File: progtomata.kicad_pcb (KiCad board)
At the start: 2 copper layers, 29 parts, among them J1 Conn_01x04_Pin, J2 Conn_01x04_Pin, P1 USB_C_Plug_USB2.0, SW1 SW_SPDT, U1 STM32F407VGTx, U2 AMS1117-3.3, U3 74LS148, Y1 8MHz

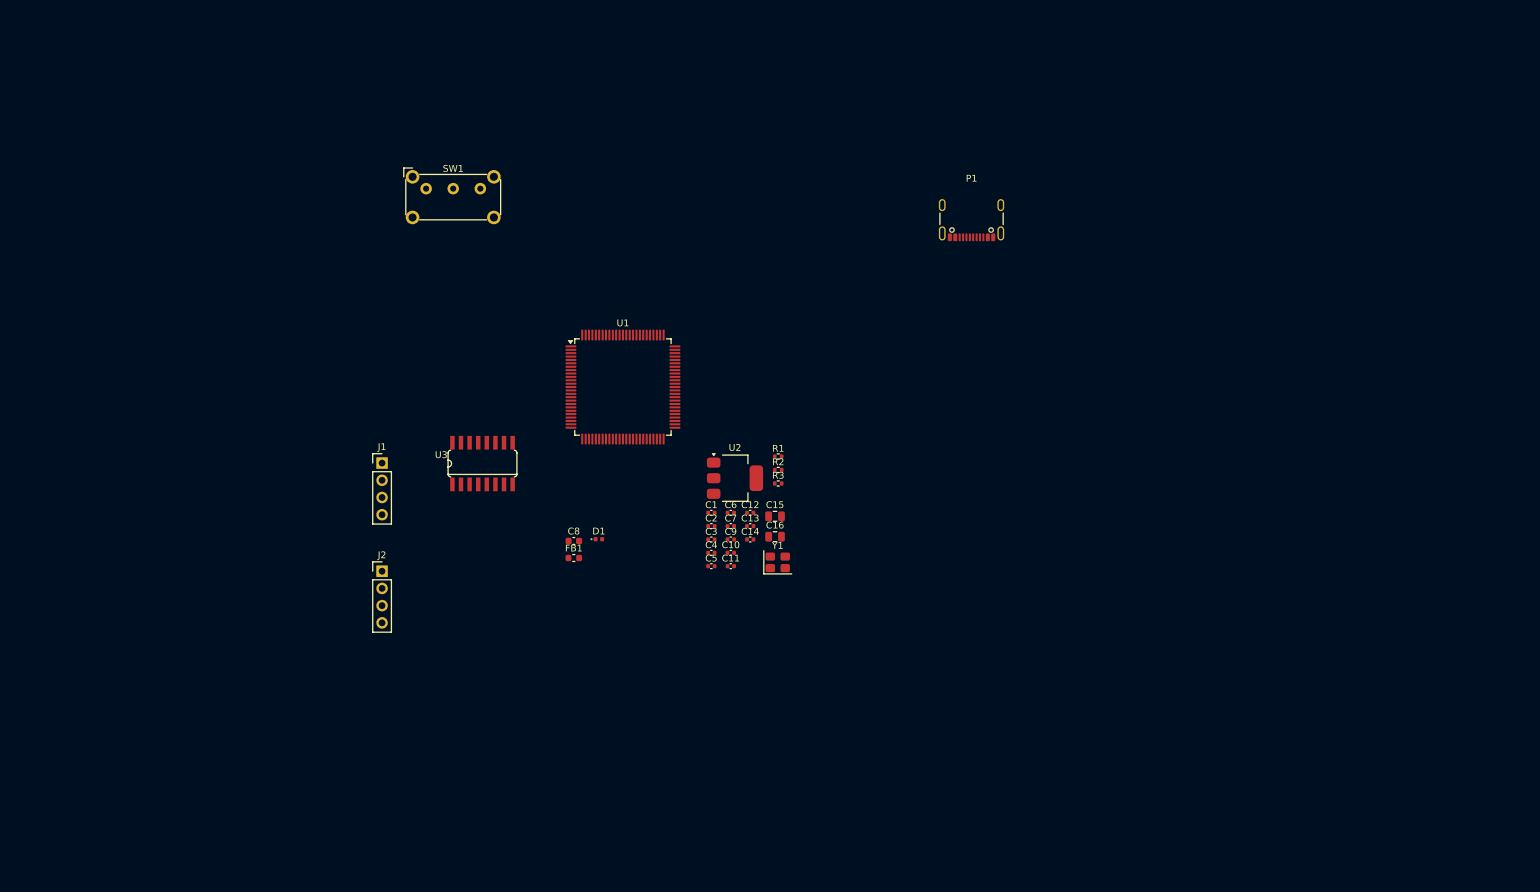
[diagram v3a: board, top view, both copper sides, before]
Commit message: Add button interface
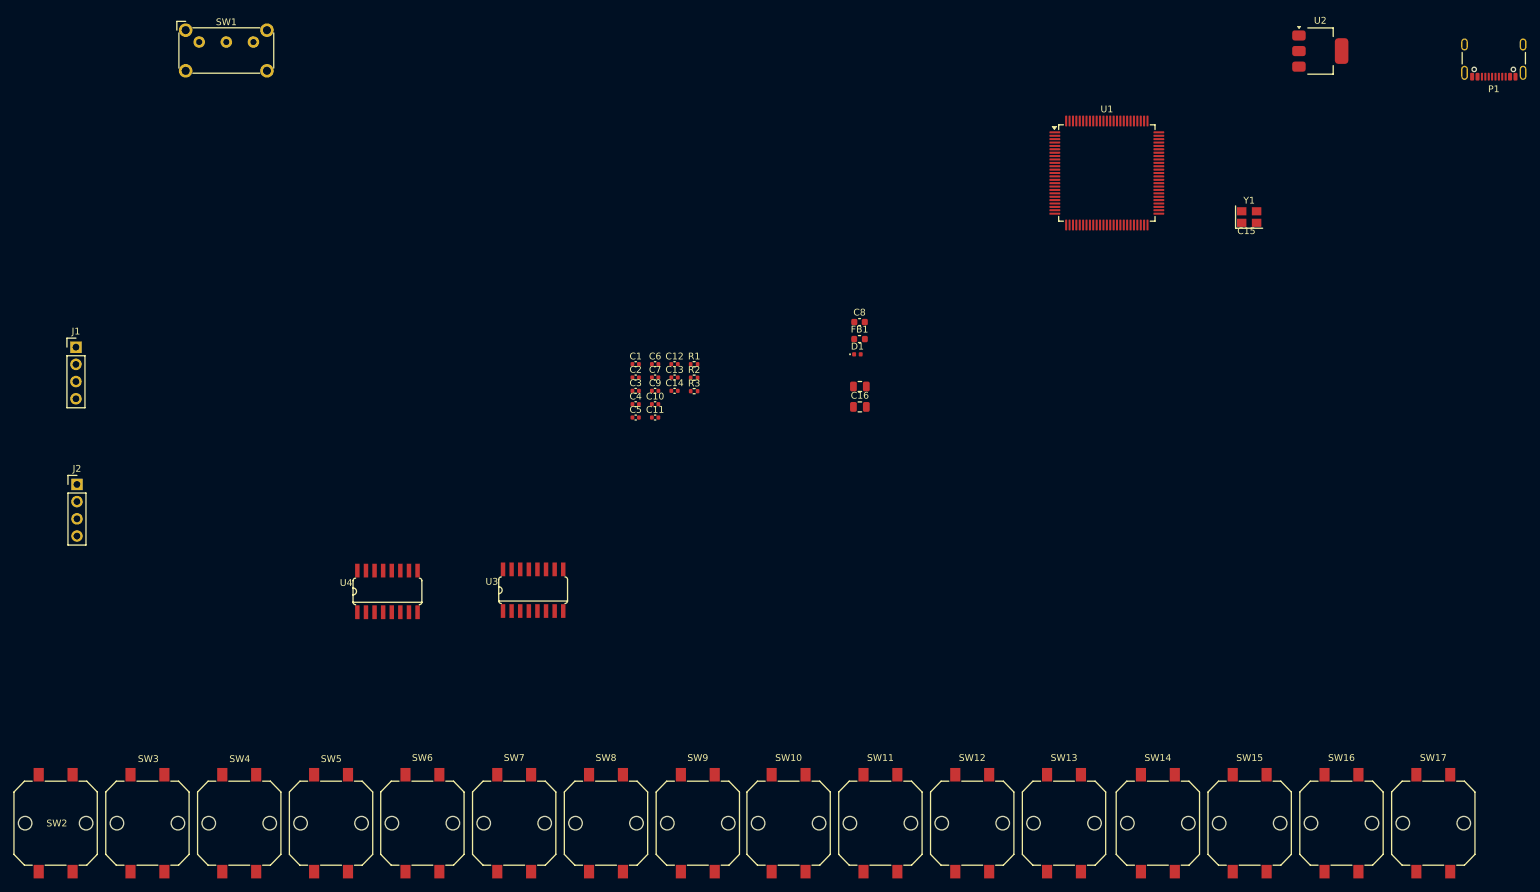
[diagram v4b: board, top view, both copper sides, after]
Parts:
- added SW10: SW_Push_LED, Button_Switch_SMD:SW_Push_1P1T_NO_CK_PTS125Sx43PSMTR, F.Cu at (143.0, 145.7)
- added SW11: SW_Push_LED, Button_Switch_SMD:SW_Push_1P1T_NO_CK_PTS125Sx43PSMTR, F.Cu at (156.6, 145.7)
- added SW12: SW_Push_LED, Button_Switch_SMD:SW_Push_1P1T_NO_CK_PTS125Sx43PSMTR, F.Cu at (170.1, 145.7)
- added SW13: SW_Push_LED, Button_Switch_SMD:SW_Push_1P1T_NO_CK_PTS125Sx43PSMTR, F.Cu at (183.7, 145.7)
- added SW14: SW_Push_LED, Button_Switch_SMD:SW_Push_1P1T_NO_CK_PTS125Sx43PSMTR, F.Cu at (197.5, 145.7)
- added SW15: SW_Push_LED, Button_Switch_SMD:SW_Push_1P1T_NO_CK_PTS125Sx43PSMTR, F.Cu at (211.1, 145.7)
- added SW16: SW_Push_LED, Button_Switch_SMD:SW_Push_1P1T_NO_CK_PTS125Sx43PSMTR, F.Cu at (224.6, 145.7)
- added SW17: SW_Push_LED, Button_Switch_SMD:SW_Push_1P1T_NO_CK_PTS125Sx43PSMTR, F.Cu at (238.2, 145.7)
- added SW2: SW_Push_LED, Button_Switch_SMD:SW_Push_1P1T_NO_CK_PTS125Sx43PSMTR, F.Cu at (34.8, 145.7)
- added SW3: SW_Push_LED, Button_Switch_SMD:SW_Push_1P1T_NO_CK_PTS125Sx43PSMTR, F.Cu at (48.4, 145.7)
- added SW4: SW_Push_LED, Button_Switch_SMD:SW_Push_1P1T_NO_CK_PTS125Sx43PSMTR, F.Cu at (61.9, 145.7)
- added SW5: SW_Push_LED, Button_Switch_SMD:SW_Push_1P1T_NO_CK_PTS125Sx43PSMTR, F.Cu at (75.5, 145.7)
- added SW6: SW_Push_LED, Button_Switch_SMD:SW_Push_1P1T_NO_CK_PTS125Sx43PSMTR, F.Cu at (89.0, 145.7)
- added SW7: SW_Push_LED, Button_Switch_SMD:SW_Push_1P1T_NO_CK_PTS125Sx43PSMTR, F.Cu at (102.5, 145.7)
- added SW8: SW_Push_LED, Button_Switch_SMD:SW_Push_1P1T_NO_CK_PTS125Sx43PSMTR, F.Cu at (116.0, 145.7)
- added SW9: SW_Push_LED, Button_Switch_SMD:SW_Push_1P1T_NO_CK_PTS125Sx43PSMTR, F.Cu at (129.6, 145.7)
- added U4: 74LS148, 74LS148:SO16, F.Cu at (83.8, 111.4)
- moved U2 106.9 mm to (221.5, 31.7)
- moved Y1 86.2 mm to (211.0, 56.2)
- moved P1 80.6 mm to (247.1, 31.8)
- moved U1 78.1 mm to (190.0, 49.7)
- moved C8 53.1 mm to (153.5, 71.7)
- moved FB1 53.1 mm to (153.5, 74.2)
- moved J1 48.3 mm to (37.8, 75.4)
- moved D1 46.9 mm to (153.2, 76.5)
- moved J2 46.8 mm to (38.0, 95.7)
- moved SW1 39.9 mm to (56.0, 30.4)
- moved C10 24.6 mm to (123.3, 83.8)
- moved C11 24.6 mm to (123.3, 85.8)
- moved C12 24.6 mm to (126.2, 77.9)
- moved C13 24.6 mm to (126.2, 79.9)
- moved C14 24.6 mm to (126.2, 81.8)
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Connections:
- C1 pad 1: +3.3V -> +5V
- C10 pad 1: +3.3VA -> +5V
- C11 pad 1: +3.3V -> +5V
- C16 pad 1: +3.3V -> +5V
- C2 pad 1: +3.3V -> +5V
- C3 pad 1: +3.3V -> +5V
- C4 pad 1: +3.3V -> +5V
- C5 pad 1: +3.3V -> +5V
- C6 pad 1: +3.3V -> +5V
- C7 pad 1: +3.3V -> +5V
- C8 pad 1: +3.3V -> +5V
- C9 pad 1: +3.3VA -> +5V
- D1 pad 2: +3.3V -> +5V
- FB1 pad 1: +3.3V -> +5V
- FB1 pad 2: +3.3VA -> +5V
- J1 pad 1: +3.3V -> +5V
- J2 pad 1: +3.3V -> +5V
- SW1 pad 3: +3.3V -> +5V
- U1 pad 100: +3.3V -> +5V
- U1 pad 11: +3.3V -> +5V
- U1 pad 19: +3.3V -> +5V
- U1 pad 22: +3.3VA -> +5V
- U1 pad 28: +3.3V -> +5V
- U1 pad 50: +3.3V -> +5V
- U1 pad 6: +3.3V -> +5V
- U1 pad 7: unconnected-(U1-PC13-Pad7) -> ENC2_Q0
- U1 pad 75: +3.3V -> +5V
- U1 pad 8: unconnected-(U1-PC14-Pad8) -> ENC2_Q1
- U1 pad 9: unconnected-(U1-PC15-Pad9) -> ENC2_Q2
- U2 pad 2: +3.3V -> +5V
- U3 pad 1: unconnected-(U3-I4-Pad1) -> ENC1_I4
- U3 pad 10: unconnected-(U3-IO-Pad10) -> ENC1_I0
- U3 pad 11: unconnected-(U3-I1-Pad11) -> ENC1_I1
- U3 pad 12: unconnected-(U3-I2-Pad12) -> ENC1_I2
- U3 pad 13: unconnected-(U3-I3-Pad13) -> ENC1_I3
- U3 pad 16: +3.3V -> +5V
- U3 pad 2: unconnected-(U3-I5-Pad2) -> ENC1_I5
- U3 pad 3: unconnected-(U3-I6-Pad3) -> ENC1_I6
- U3 pad 4: unconnected-(U3-I7-Pad4) -> ENC1_I7
